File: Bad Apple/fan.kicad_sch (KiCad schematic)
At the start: 5 parts, among them J2 Conn_01x02

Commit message: chore(pcb): metadata stuff
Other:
- company: (none) -> Mixed Engineering Group 3 | STEM 12-Altruism / AY 2526 | CIT-U SHS
- title: (none) -> Autonomous  Courier Robot "Bad Apple"
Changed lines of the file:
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@@
 	(generator_version "9.0")
 	(paper "A4")
+	(title_block
+		(title "Autonomous  Courier Robot \"Bad Apple\"")
+		(date "2025-08-28")
+		(rev "1")
+		(company "Mixed Engineering Group 3 | STEM 12-Altruism / AY 2526 | CIT-U SHS")
+		(comment 4 "CPU Fan")
+	)
 	(text "Fan\n\nA hole should be created somewhere\nfor the fan. Mounting holes should\nalso be added to make sure the fan\nhas somewhere to be mounted on"
 		(exclude_from_sim no)

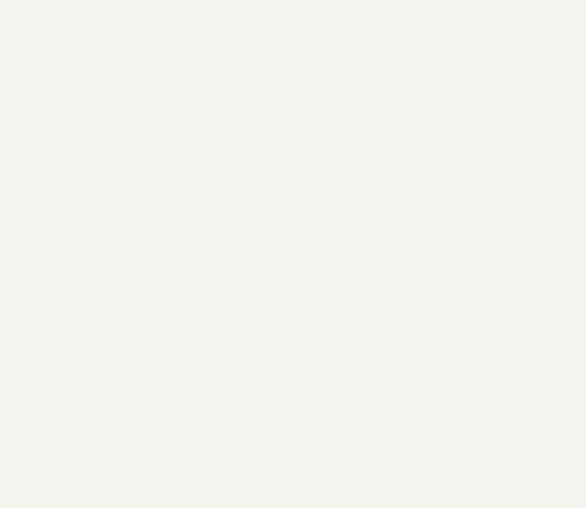
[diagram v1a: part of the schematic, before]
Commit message: feat(pcb): motor subsystem
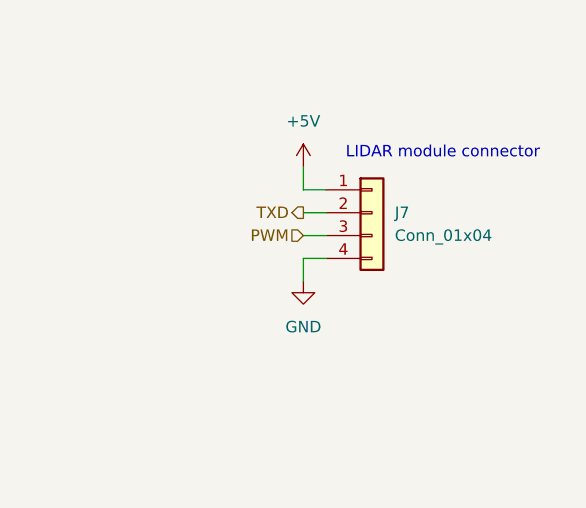
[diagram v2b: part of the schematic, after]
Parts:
- added J7: Conn_01x04, symbol Connector_Generic:Conn_01x04
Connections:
- net +5V: now also J7.1 (Pin_1)
- net GND: now also J7.4 (Pin_4)
- new net PWM: J7.3 (Pin_3)
- new net TXD: J7.2 (Pin_2)
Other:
- note added: "LIDAR module connector"

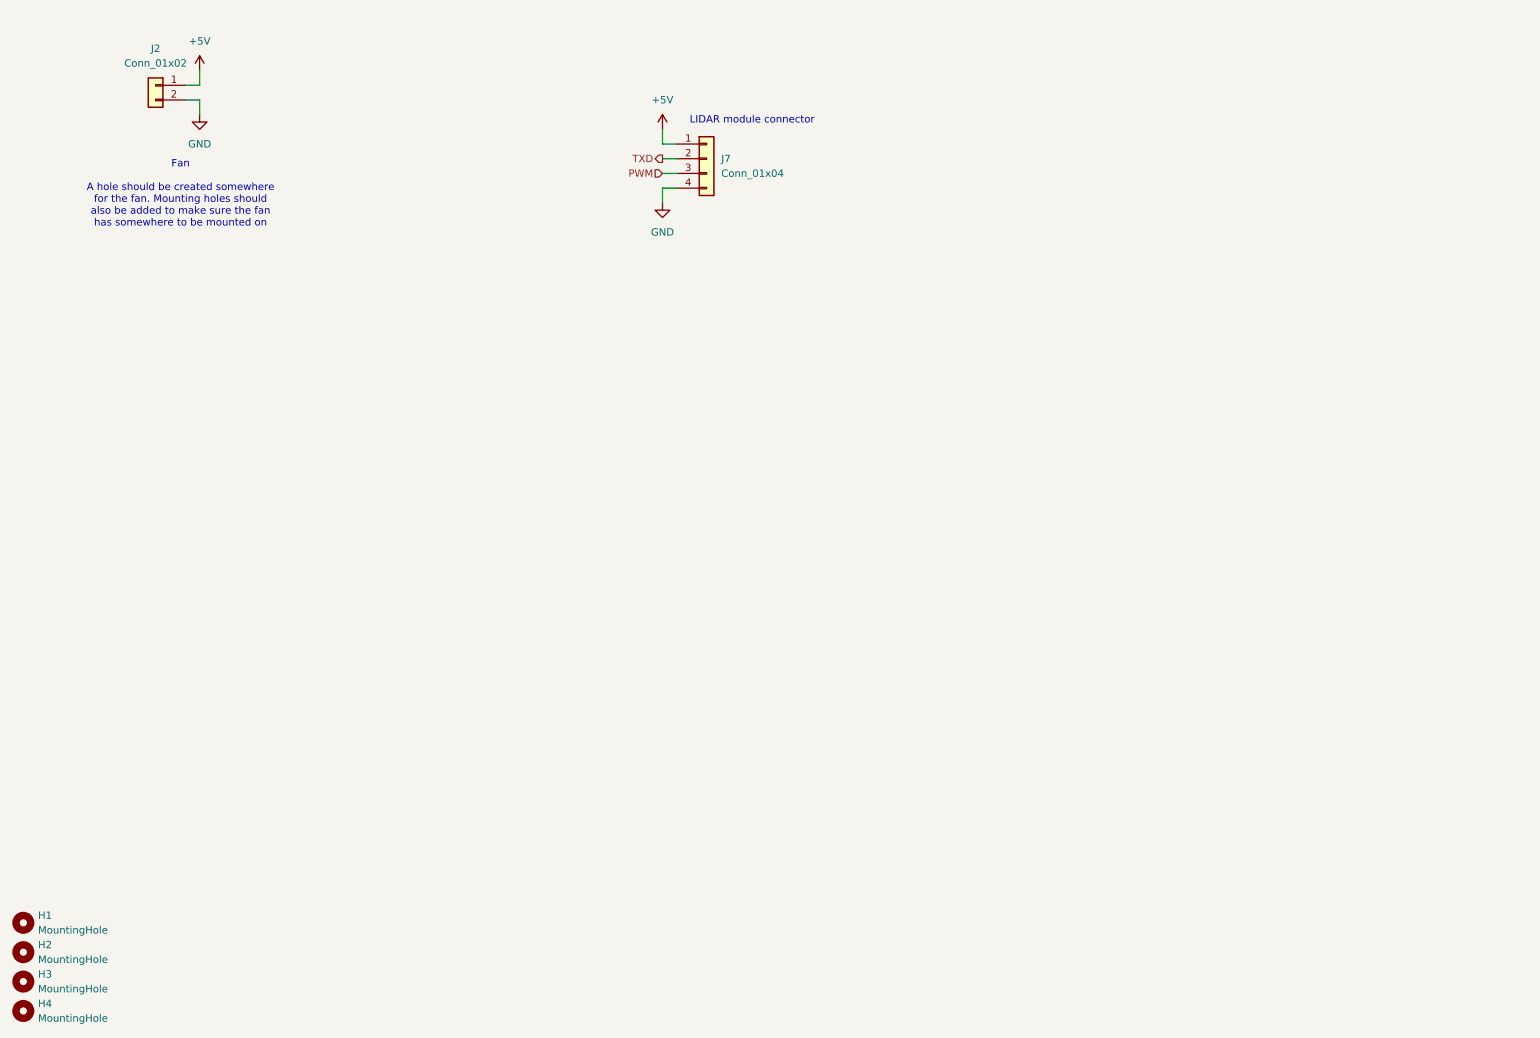
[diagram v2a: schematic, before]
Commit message: feat(pcb): added PCA9685 I2C LED Driver as the driver for the servo motors
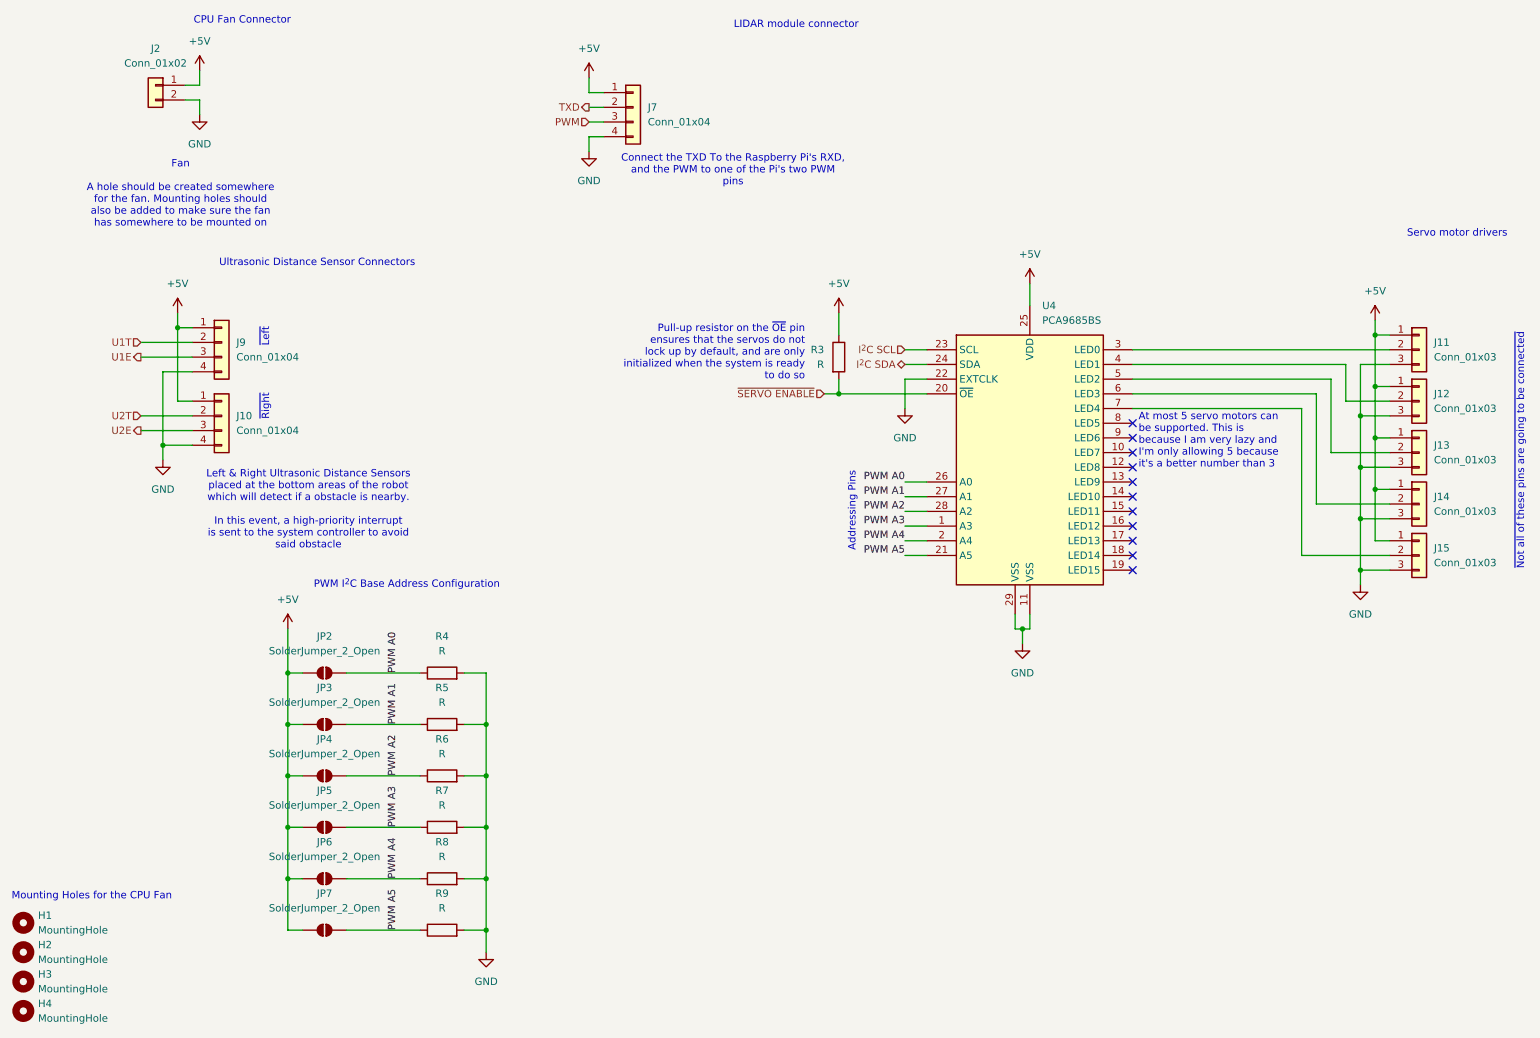
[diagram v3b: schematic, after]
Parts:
- added J10, J9: Conn_01x04, symbol Connector_Generic:Conn_01x04
- added J11, J12, J13, J14, J15: Conn_01x03, symbol Connector_Generic:Conn_01x03
- added JP2, JP3, JP4, JP5, JP6, JP7: SolderJumper_2_Open, symbol Jumper:SolderJumper_2_Open
- added R3, R4, R5, R6, R7, R8, R9: R, symbol Device:R
- added U4: PCA9685BS, Package_DFN_QFN:QFN-28-1EP_6x6mm_P0.65mm_EP4.25x4.25mm, symbol Driver_LED:PCA9685BS
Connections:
- net +5V: now also J10.1 (Pin_1), J11.1 (Pin_1), J12.1 (Pin_1), J13.1 (Pin_1), J14.1 (Pin_1), J15.1 (Pin_1), J9.1 (Pin_1), JP2.1 (A), JP3.1 (A), JP4.1 (A), JP5.1 (A), JP6.1 (A), JP7.1 (A), R3.1, U4.25 (VDD)
- net GND: now also J10.4 (Pin_4), J11.3 (Pin_3), J12.3 (Pin_3), J13.3 (Pin_3), J14.3 (Pin_3), J15.3 (Pin_3), J9.4 (Pin_4), R4.2, R5.2, R6.2, R7.2, R8.2, R9.2, U4.11 (VSS), U4.22 (EXTCLK), U4.29 (VSS)
- new net: J11.2 (Pin_2), U4.3 (LED0)
- new net: J12.2 (Pin_2), U4.4 (LED1)
- new net: J13.2 (Pin_2), U4.5 (LED2)
- new net: J14.2 (Pin_2), U4.6 (LED3)
- new net: J15.2 (Pin_2), U4.7 (LED4)
- new net I^{2}C SCL: U4.23 (SCL)
- new net I^{2}C SDA: U4.24 (SDA)
- new net PWM A0: JP2.2 (B), R4.1, U4.26 (A0)
- new net PWM A1: JP3.2 (B), R5.1, U4.27 (A1)
- new net PWM A2: JP4.2 (B), R6.1, U4.28 (A2)
- new net PWM A3: JP5.2 (B), R7.1, U4.1 (A3)
- new net PWM A4: JP6.2 (B), R8.1, U4.2 (A4)
- new net PWM A5: JP7.2 (B), R9.1, U4.21 (A5)
- new net U1E: J9.3 (Pin_3)
- new net U1T: J9.2 (Pin_2)
- new net U2E: J10.3 (Pin_3)
- new net U2T: J10.2 (Pin_2)
- new net ~{SERVO ENABLE}: R3.2, U4.20 (~{OE})
- no-connect marks 0 -> 11
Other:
- note added: "Addressing Pins"
- note added: "At most 5 servo motors can be supported. This is because I am very lazy and I'm only allowing 5 because it's a better number than 3"
- note added: "CPU Fan Connector"
- note added: "Connect the TXD To the Raspberry Pi's RXD, and the PWM to one of the Pi's two PWM pins"
- note added: "Left & Right Ultrasonic Distance Sensors placed at the bottom areas of the robot which will detect if a obstacle is nearby. In this event, a high-priority interrupt is sent to the system controller to avoid said obstacle"
- note added: "Mounting Holes for the CPU Fan"
- note added: "PWM I^{2}C Base Address Configuration"
- note added: "Pull-up resistor on the ~{OE} pin ensures that the servos do not lock up by default, and are only initialized when the system is ready to do so"
- note added: "Servo motor drivers"
- note added: "Ultrasonic Distance Sensor Connectors"
- note added: "~{Left}"
- note added: "~{Not all of these pins are going to be connected}"
- note added: "~{Right}"
- moved on the sheet: J7

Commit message: feat(pcb): i forgor ☠️
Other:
- moved on the sheet: H1, H2, H3, H4
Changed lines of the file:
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@@
 	(text "Mounting Holes for the CPU Fan"
 		(exclude_from_sim no)
-		(at 15.748 171.958 0)
+		(at 86.868 24.638 0)
 		(effects
 			(font
 				(size 1.27 1.27)
 			)
-			(justify left)
+			(justify right)
 		)
 	)
@@
 		(polyline
 			(pts
-				(xy 25.4 57.15) (xy 64.77 57.15) (xy 64.77 21.59) (xy 25.4 21.59)
+				(xy 25.4 57.15) (xy 88.9 57.15) (xy 88.9 21.59) (xy 25.4 21.59)
 			)
 			(stroke
@@
 	(symbol
 		(lib_id "Mechanical:MountingHole")
-		(at 17.78 176.53 0)
+		(at 85.09 29.21 0)
+		(mirror y)
 		(unit 1)
 		(exclude_from_sim no)
@@
 		(fields_autoplaced yes)
 		(property "Reference" "H1"
-			(at 20.32 175.2599 0)
+			(at 82.55 27.9399 0)
 			(effects
 				(font
@@
 		)
 		(property "Value" "MountingHole"
-			(at 20.32 177.7999 0)
+			(at 82.55 30.4799 0)
 			(effects
 				(font
@@
 		)
 		(property "Footprint" "Connector_JST:JST_ACH_BM01B-ACHSS-A-GAN-ETF_1x01-1MP_P1.20mm_Vertical"
-			(at 17.78 176.53 0)
+			(at 85.09 29.21 0)
 			(effects
 				(font
@@
 		)
 		(property "Datasheet" "~"
-			(at 17.78 176.53 0)
+			(at 85.09 29.21 0)
 			(effects
 				(font
@@
 		)
 		(property "Description" "Mounting Hole without connection"
-			(at 17.78 176.53 0)
+			(at 85.09 29.21 0)
 			(effects
 				(font
@@
 	(symbol
 		(lib_id "Mechanical:MountingHole")
-		(at 17.78 181.61 0)
+		(at 85.09 34.29 0)
+		(mirror y)
 		(unit 1)
 		(exclude_from_sim no)
@@
 		(fields_autoplaced yes)
 		(property "Reference" "H2"
-			(at 20.32 180.3399 0)
+			(at 82.55 33.0199 0)
 			(effects
 				(font
@@
 		)
 		(property "Value" "MountingHole"
-			(at 20.32 182.8799 0)
+			(at 82.55 35.5599 0)
 			(effects
 				(font
@@
 		)
 		(property "Footprint" "Connector_JST:JST_ACH_BM01B-ACHSS-A-GAN-ETF_1x01-1MP_P1.20mm_Vertical"
-			(at 17.78 181.61 0)
+			(at 85.09 34.29 0)
 			(effects
 				(font
@@
 		)
 		(property "Datasheet" "~"
-			(at 17.78 181.61 0)
+			(at 85.09 34.29 0)
 			(effects
 				(font
@@
 		)
 		(property "Description" "Mounting Hole without connection"
-			(at 17.78 181.61 0)
+			(at 85.09 34.29 0)
 			(effects
 				(font
@@
 	(symbol
 		(lib_id "Mechanical:MountingHole")
-		(at 17.78 186.69 0)
+		(at 85.09 39.37 0)
+		(mirror y)
 		(unit 1)
 		(exclude_from_sim no)
@@
 		(fields_autoplaced yes)
 		(property "Reference" "H3"
-			(at 20.32 185.4199 0)
+			(at 82.55 38.0999 0)
 			(effects
 				(font
@@
 		)
 		(property "Value" "MountingHole"
-			(at 20.32 187.9599 0)
+			(at 82.55 40.6399 0)
 			(effects
 				(font
@@
 		)
 		(property "Footprint" "Connector_JST:JST_ACH_BM01B-ACHSS-A-GAN-ETF_1x01-1MP_P1.20mm_Vertical"
-			(at 17.78 186.69 0)
+			(at 85.09 39.37 0)
 			(effects
 				(font
@@
 		)
 		(property "Datasheet" "~"
-			(at 17.78 186.69 0)
+			(at 85.09 39.37 0)
 			(effects
 				(font
@@
 		)
 		(property "Description" "Mounting Hole without connection"
-			(at 17.78 186.69 0)
+			(at 85.09 39.37 0)
 			(effects
 				(font
@@
 	(symbol
 		(lib_id "Mechanical:MountingHole")
-		(at 17.78 191.77 0)
+		(at 85.09 44.45 0)
+		(mirror y)
 		(unit 1)
 		(exclude_from_sim no)
@@
 		(fields_autoplaced yes)
 		(property "Reference" "H4"
-			(at 20.32 190.4999 0)
+			(at 82.55 43.1799 0)
 			(effects
 				(font
@@
 		)
 		(property "Value" "MountingHole"
-			(at 20.32 193.0399 0)
+			(at 82.55 45.7199 0)
 			(effects
 				(font
@@
 		)
 		(property "Footprint" "Connector_JST:JST_ACH_BM01B-ACHSS-A-GAN-ETF_1x01-1MP_P1.20mm_Vertical"
-			(at 17.78 191.77 0)
+			(at 85.09 44.45 0)
 			(effects
 				(font
@@
 		)
 		(property "Datasheet" "~"
-			(at 17.78 191.77 0)
+			(at 85.09 44.45 0)
 			(effects
 				(font
@@
 		)
 		(property "Description" "Mounting Hole without connection"
-			(at 17.78 191.77 0)
+			(at 85.09 44.45 0)
 			(effects
 				(font

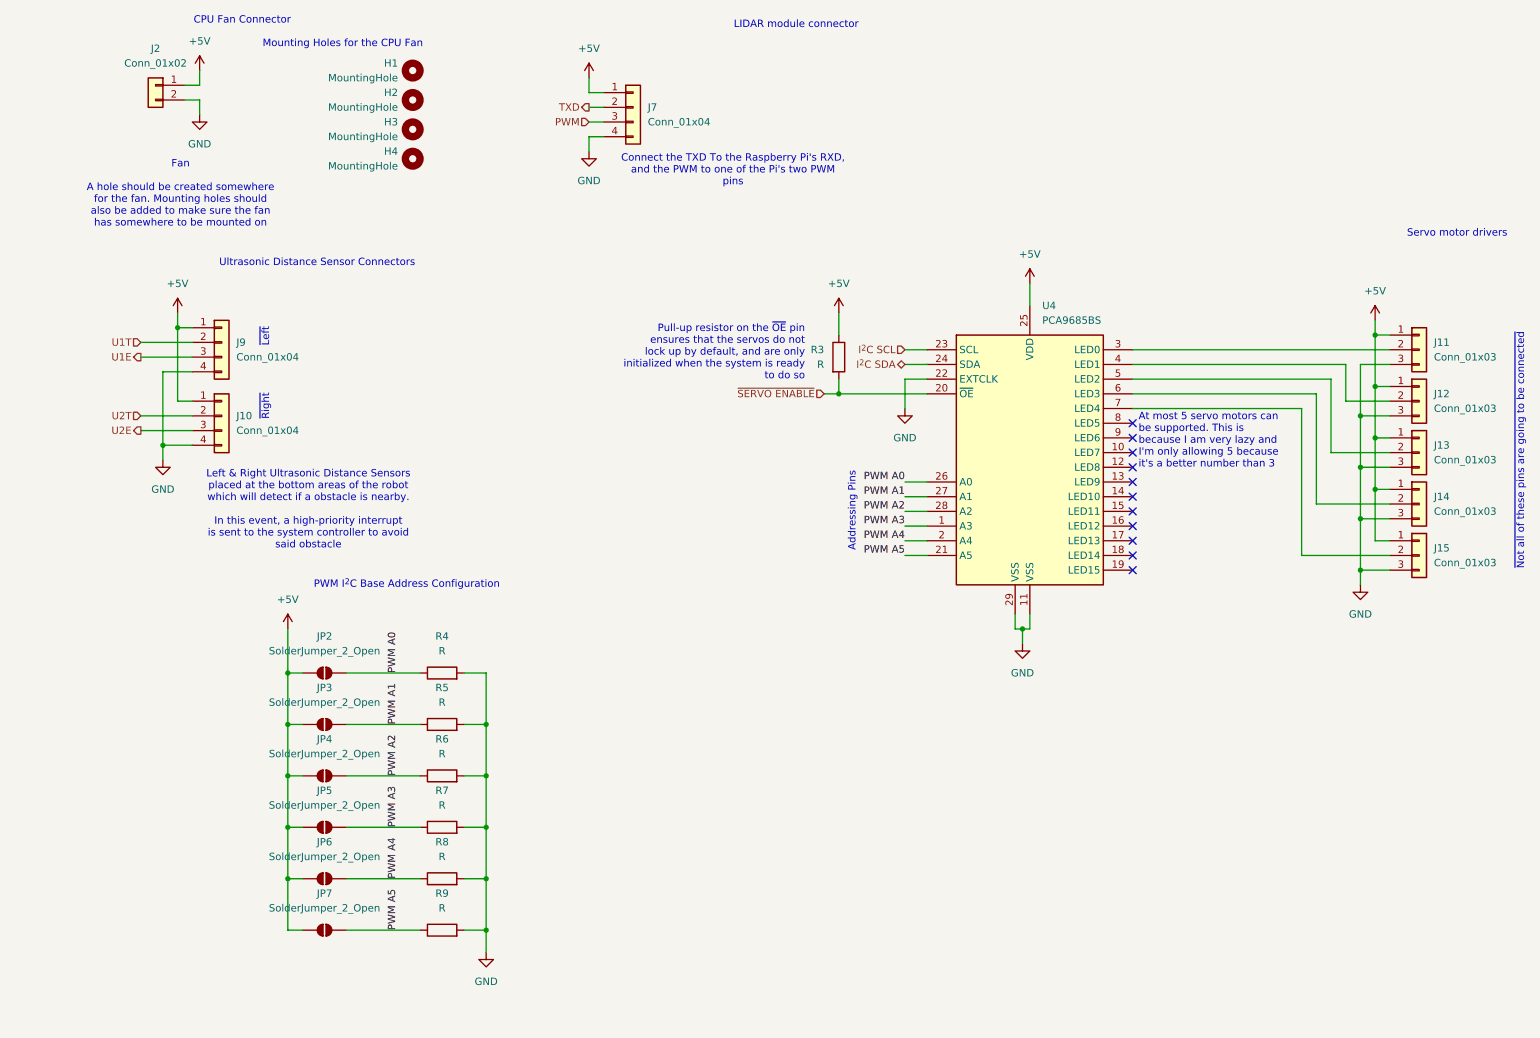
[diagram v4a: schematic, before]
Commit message: feat(pcb): more hierarchy
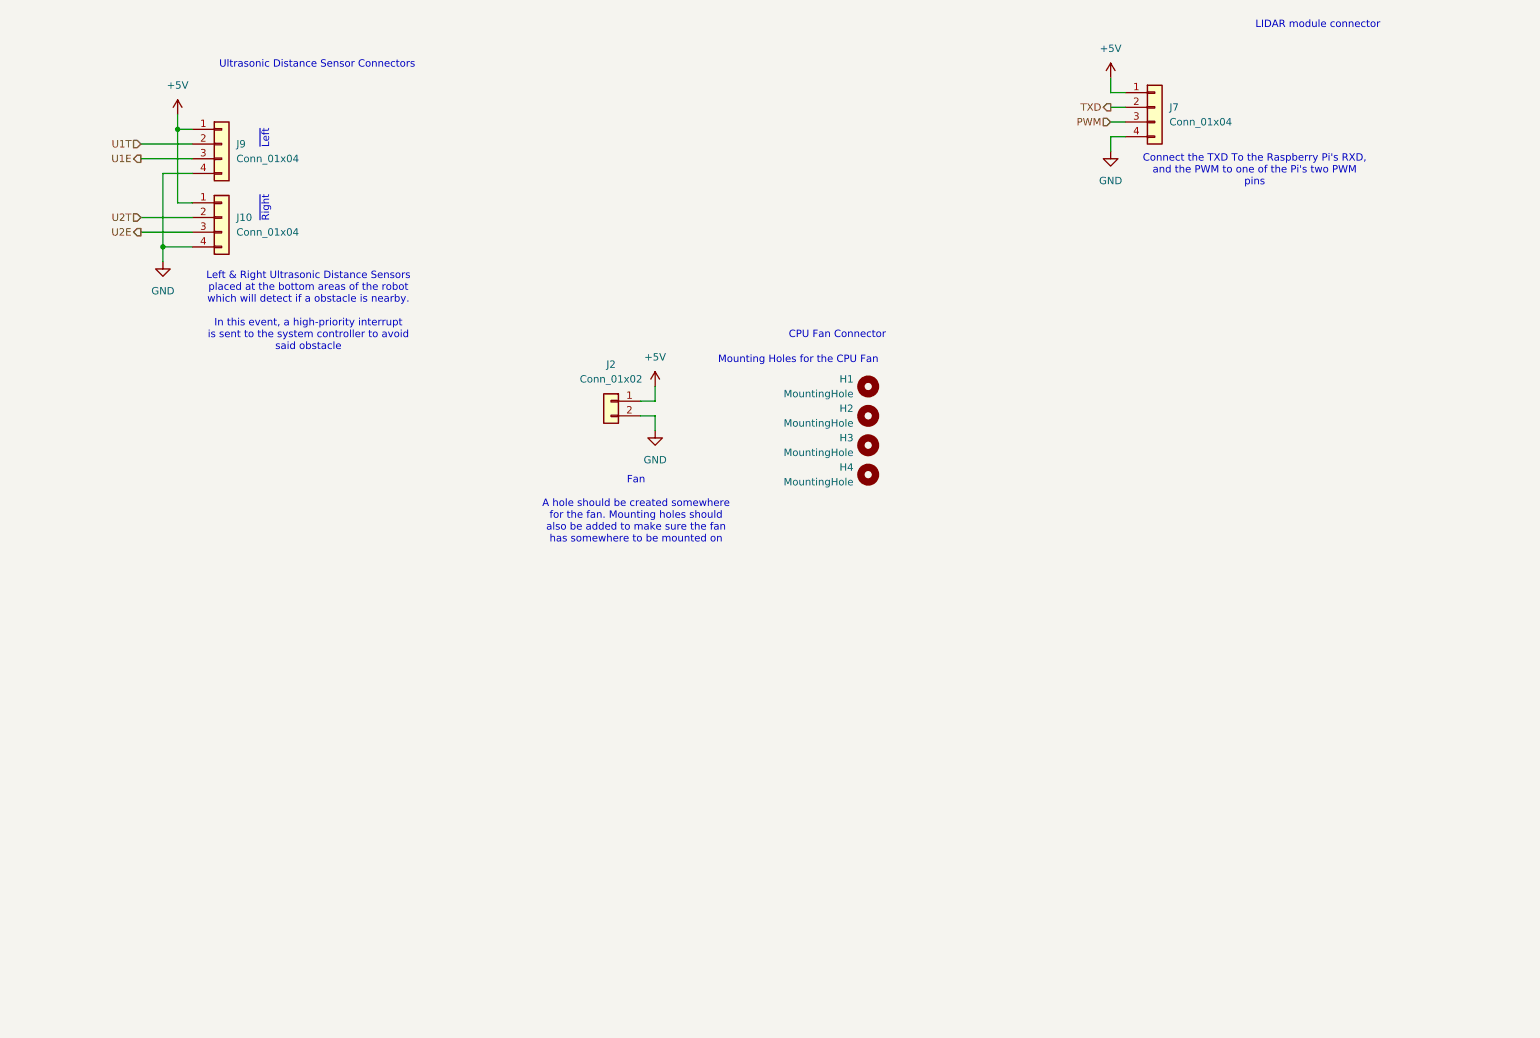
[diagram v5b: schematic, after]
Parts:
- removed J11, J12, J13, J14, J15: Conn_01x03, symbol Connector_Generic:Conn_01x03
- removed JP2, JP3, JP4, JP5, JP6, JP7: SolderJumper_2_Open, symbol Jumper:SolderJumper_2_Open
- removed R3, R4, R5, R6, R7, R8, R9: R, symbol Device:R
- removed U4: PCA9685BS, Package_DFN_QFN:QFN-28-1EP_6x6mm_P0.65mm_EP4.25x4.25mm, symbol Driver_LED:PCA9685BS
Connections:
- no-connect marks 11 -> 0
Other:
- note removed: "Addressing Pins"
- note removed: "At most 5 servo motors can be supported. This is because I am very lazy and I'm only allowing 5 because it's a better number than 3"
- note removed: "PWM I^{2}C Base Address Configuration"
- note removed: "Pull-up resistor on the ~{OE} pin ensures that the servos do not lock up by default, and are only initialized when the system is ready to do so"
- note removed: "Servo motor drivers"
- note removed: "~{Not all of these pins are going to be connected}"
- moved on the sheet: H1, H2, H3, H4, J10, J2, J7, J9
